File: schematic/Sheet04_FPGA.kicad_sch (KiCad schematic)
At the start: 6 parts

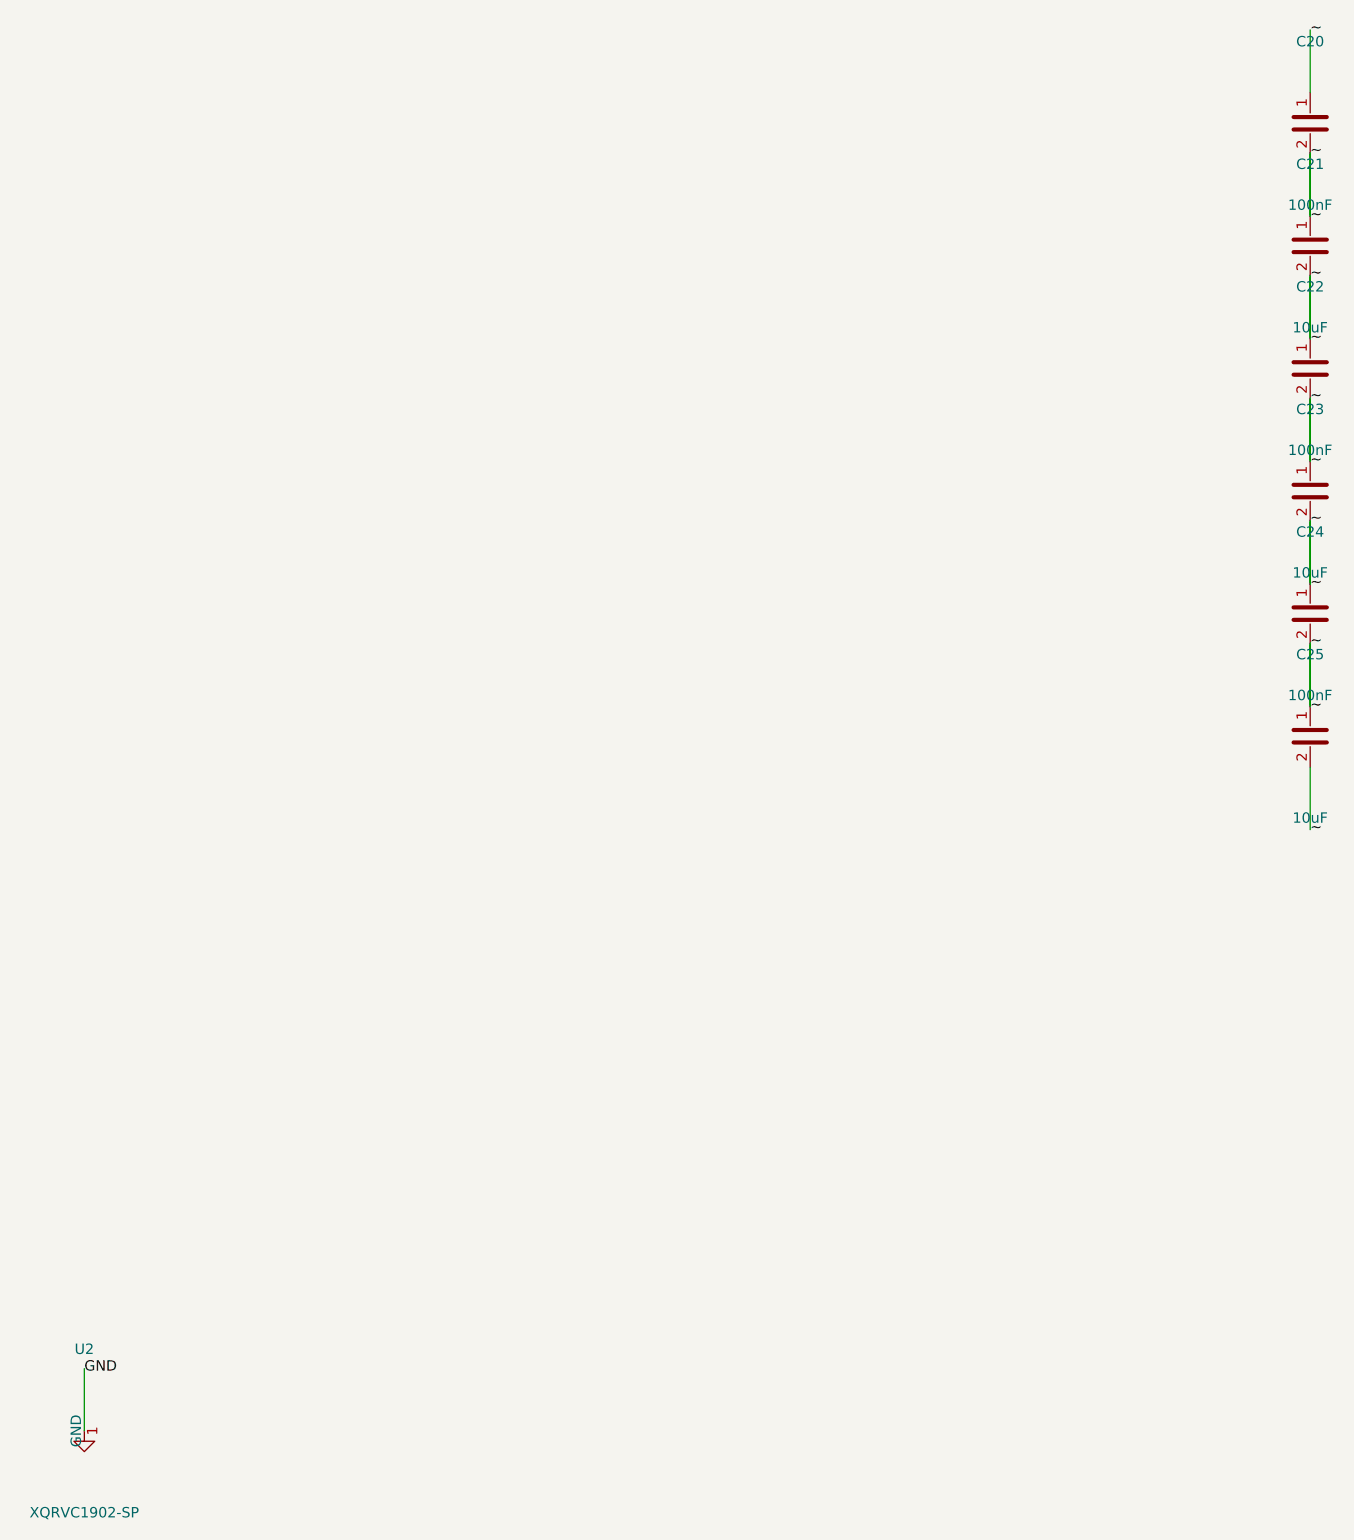
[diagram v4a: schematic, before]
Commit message: fix: use horizontal wire stubs to prevent KiCad net merging
Root cause: vertical wires from stacked power pins (1.27mm spacing)
overlapped when wire length > pin spacing, causing KiCad to merge
all power nets into one. Also skip unnamed (~) passive component pins.

Changes:
- Always use horizontal LEFT stubs regardless of pin angle
- Skip pins with net_name '~' (capacitor/resistor unnamed pins)
- 557 pin connections across 13 sheets, all pass KiCad CLI

NOTE: power net separation still shows all power_in pins on one net
in kicad-cli netlist export - needs further investigation.
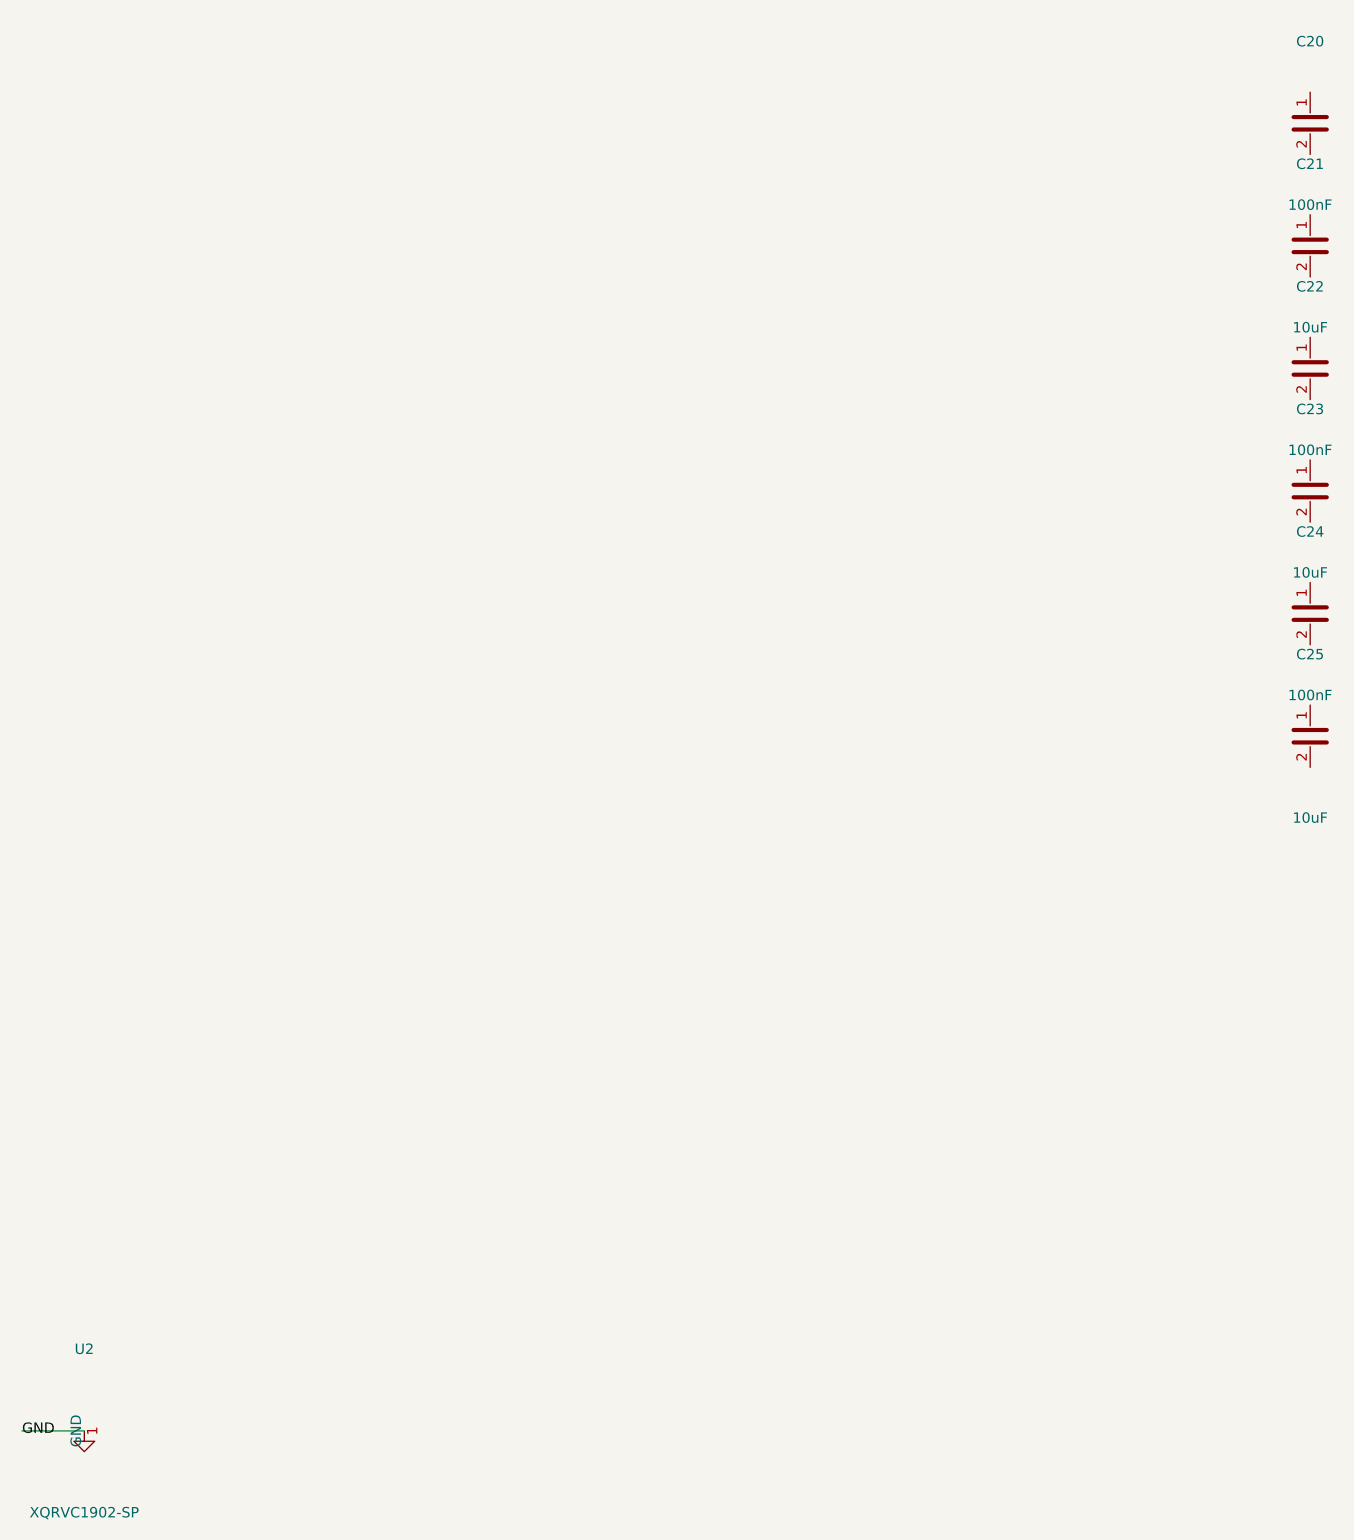
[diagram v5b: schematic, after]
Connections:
- removed net ~: C20.1, C20.2, C21.1, C21.2, C22.1, C22.2, C23.1, C23.2, C24.1, C24.2, C25.1, C25.2
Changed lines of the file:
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@@
     (pin "2")
   )
-  (wire (pts (xy 200.0000 200.0000) (xy 200.0000 192.3800)) (stroke (width 0) (type default)))
-  (label "GND" (at 200.0000 192.3800 0) (effects (font (size 1.27 1.27))))
-  (wire (pts (xy 350.0000 36.1900) (xy 350.0000 28.5700)) (stroke (width 0) (type default)))
-  (label "~" (at 350.0000 28.5700 0) (effects (font (size 1.27 1.27))))
-  (wire (pts (xy 350.0000 43.8100) (xy 350.0000 51.4300)) (stroke (width 0) (type default)))
-  (label "~" (at 350.0000 51.4300 0) (effects (font (size 1.27 1.27))))
-  (wire (pts (xy 350.0000 51.1900) (xy 350.0000 43.5700)) (stroke (width 0) (type default)))
-  (label "~" (at 350.0000 43.5700 0) (effects (font (size 1.27 1.27))))
-  (wire (pts (xy 350.0000 58.8100) (xy 350.0000 66.4300)) (stroke (width 0) (type default)))
-  (label "~" (at 350.0000 66.4300 0) (effects (font (size 1.27 1.27))))
-  (wire (pts (xy 350.0000 66.1900) (xy 350.0000 58.5700)) (stroke (width 0) (type default)))
-  (label "~" (at 350.0000 58.5700 0) (effects (font (size 1.27 1.27))))
-  (wire (pts (xy 350.0000 73.8100) (xy 350.0000 81.4300)) (stroke (width 0) (type default)))
-  (label "~" (at 350.0000 81.4300 0) (effects (font (size 1.27 1.27))))
-  (wire (pts (xy 350.0000 81.1900) (xy 350.0000 73.5700)) (stroke (width 0) (type default)))
-  (label "~" (at 350.0000 73.5700 0) (effects (font (size 1.27 1.27))))
-  (wire (pts (xy 350.0000 88.8100) (xy 350.0000 96.4300)) (stroke (width 0) (type default)))
-  (label "~" (at 350.0000 96.4300 0) (effects (font (size 1.27 1.27))))
-  (wire (pts (xy 350.0000 96.1900) (xy 350.0000 88.5700)) (stroke (width 0) (type default)))
-  (label "~" (at 350.0000 88.5700 0) (effects (font (size 1.27 1.27))))
-  (wire (pts (xy 350.0000 103.8100) (xy 350.0000 111.4300)) (stroke (width 0) (type default)))
-  (label "~" (at 350.0000 111.4300 0) (effects (font (size 1.27 1.27))))
-  (wire (pts (xy 350.0000 111.1900) (xy 350.0000 103.5700)) (stroke (width 0) (type default)))
-  (label "~" (at 350.0000 103.5700 0) (effects (font (size 1.27 1.27))))
-  (wire (pts (xy 350.0000 118.8100) (xy 350.0000 126.4300)) (stroke (width 0) (type default)))
-  (label "~" (at 350.0000 126.4300 0) (effects (font (size 1.27 1.27))))
+  (wire (pts (xy 200.0000 200.0000) (xy 192.3800 200.0000)) (stroke (width 0) (type default)))
+  (label "GND" (at 192.3800 200.0000 0) (effects (font (size 1.27 1.27))))
   (sheet_instances (path "/" (page "1")))
 )

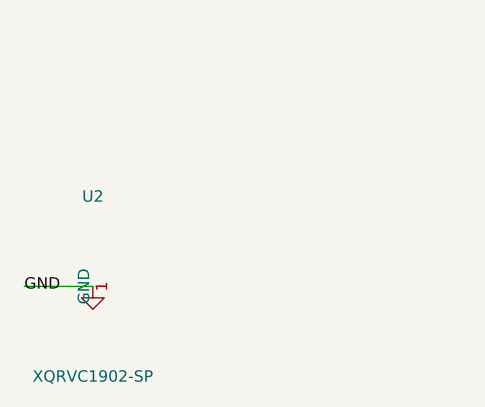
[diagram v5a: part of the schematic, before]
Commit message: fix: replace wire stubs with labels-only to prevent power net shorts
Labels placed directly at pin endpoints eliminate wire overlap that
caused BGA power pins (VA11, VA19, VD11, AGND, DGND) to merge into
a single net. Verified via netlist: GND=52, +1V0_ANA=12, +1V9_ANA=12,
+1V1_DIG=10 nodes (all correct per datasheet pin mapping).
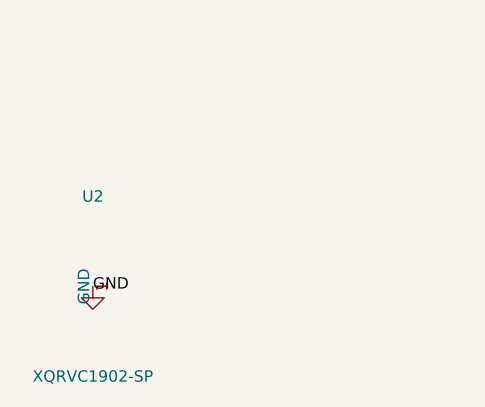
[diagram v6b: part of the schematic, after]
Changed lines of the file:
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@@
     (pin "2")
   )
-  (wire (pts (xy 200.0000 200.0000) (xy 192.3800 200.0000)) (stroke (width 0) (type default)))
-  (label "GND" (at 192.3800 200.0000 0) (effects (font (size 1.27 1.27))))
+  (label "GND" (at 200.0000 200.0000 0) (effects (font (size 1.27 1.27))))
   (sheet_instances (path "/" (page "1")))
 )
